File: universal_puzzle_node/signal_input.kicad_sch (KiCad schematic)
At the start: 3 parts

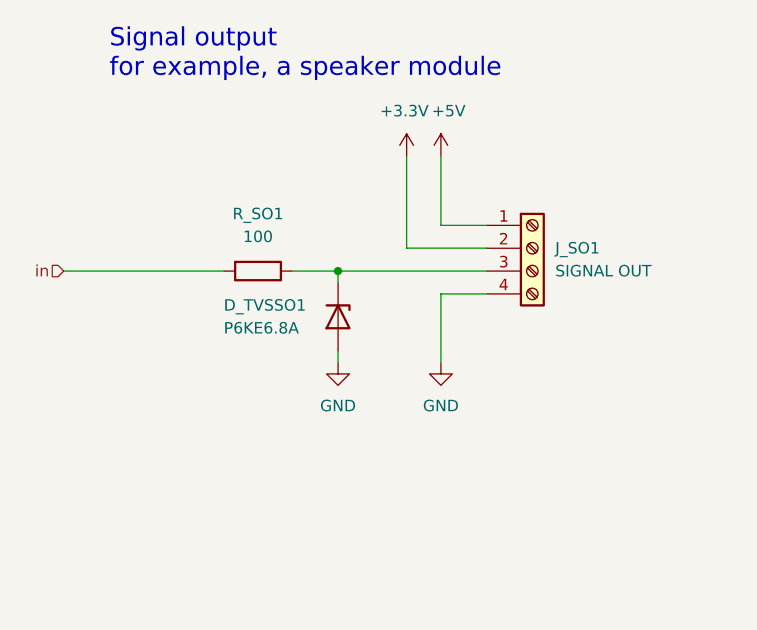
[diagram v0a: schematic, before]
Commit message: chore: rename to universal puzzle node everywhere
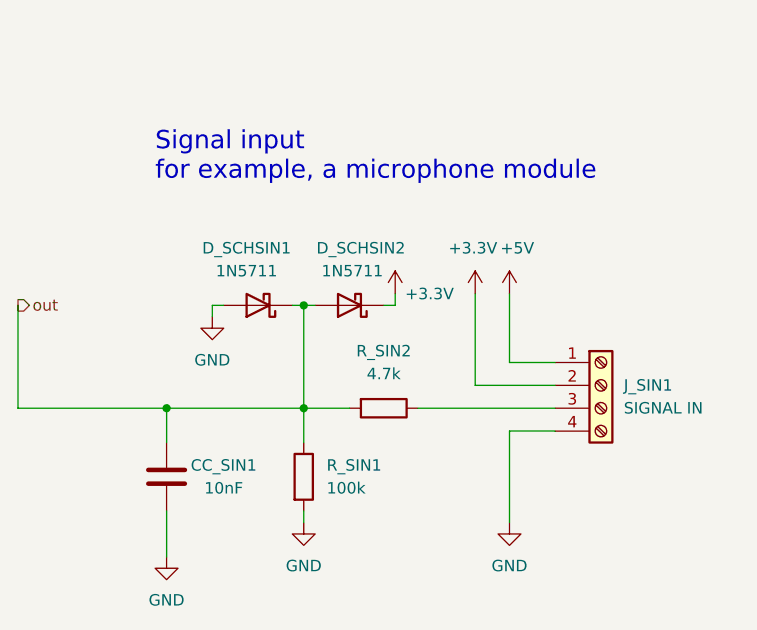
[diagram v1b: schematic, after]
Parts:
- removed D_TVSSO1: P6KE6.8A, Diode_THT:D_DO-15_P12.70mm_Horizontal, symbol Diode:PTVS5V0Z1USK
- removed J_SO1: SIGNAL OUT, TerminalBlock_Phoenix:TerminalBlock_Phoenix_MKDS-1,5-4-5.08_1x04_P5.08mm_Horizontal, symbol Connector:Screw_Terminal_01x04
- removed R_SO1: 100, Resistor_THT:R_Axial_DIN0207_L6.3mm_D2.5mm_P10.16mm_Horizontal, symbol Device:R
- added CC_SIN1: 10nF, Capacitor_THT:C_Disc_D5.0mm_W2.5mm_P5.00mm, symbol Device:C
- added D_SCHSIN1, D_SCHSIN2: 1N5711, Diode_THT:D_DO-35_SOD27_P7.62mm_Horizontal, symbol Diode:1N5711
- added J_SIN1: SIGNAL IN, TerminalBlock_Phoenix:TerminalBlock_Phoenix_MKDS-1,5-4-5.08_1x04_P5.08mm_Horizontal, symbol Connector:Screw_Terminal_01x04
- added R_SIN1: 100k, Resistor_THT:R_Axial_DIN0207_L6.3mm_D2.5mm_P10.16mm_Horizontal, symbol Device:R
- added R_SIN2: 4.7k, Resistor_THT:R_Axial_DIN0207_L6.3mm_D2.5mm_P10.16mm_Horizontal, symbol Device:R
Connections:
- net +3.3V: now also D_SCHSIN2.1 (K), J_SIN1.2 (Pin_2)
- net +5V: now also J_SIN1.1 (Pin_1)
- net GND: now also CC_SIN1.2, D_SCHSIN1.2 (A), J_SIN1.4 (Pin_4), R_SIN1.2
- new net: J_SIN1.3 (Pin_3), R_SIN2.1
- new net out: CC_SIN1.1, D_SCHSIN1.1 (K), D_SCHSIN2.2 (A), R_SIN1.1, R_SIN2.2
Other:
- note added: "Signal input for example, a microphone module"
- note removed: "Signal output for example, a speaker module"
- title: ESP digital signal output (like a speaker module) -> Signal input
